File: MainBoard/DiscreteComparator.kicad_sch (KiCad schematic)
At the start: 27 parts, among them Q17 BC557, Q18 BC557, Q19 BC557, Q20 BC557, Q21 BC557, Q22 BC557, Q23 BC557, Q24 BC557, Q25 BC557, Q26 BC547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

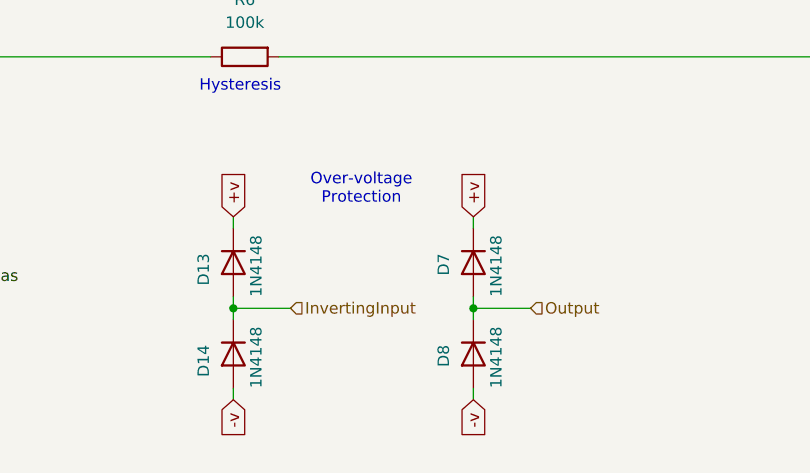
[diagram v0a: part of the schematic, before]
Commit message: added over-voltage protection on all inputs and outputs
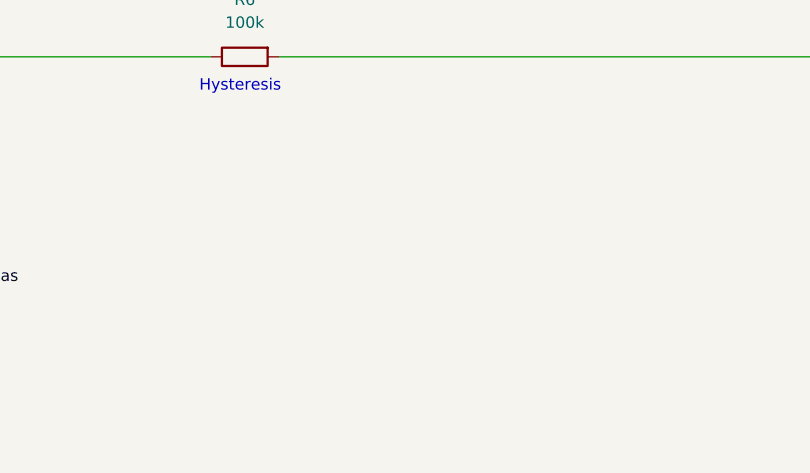
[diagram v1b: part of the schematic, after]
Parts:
- removed D13, D14, D7, D8: 1N4148, Diode_THT:D_DO-35_SOD27_P7.62mm_Horizontal, symbol Device:D
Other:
- note removed: "Over-voltage Protection"

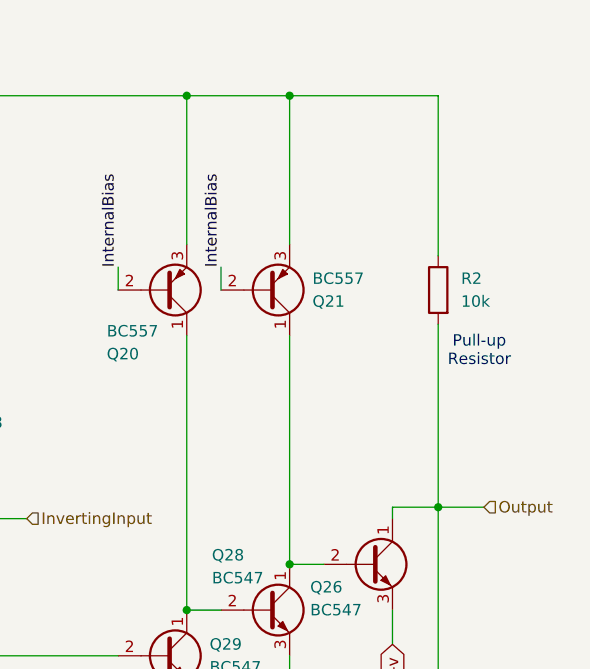
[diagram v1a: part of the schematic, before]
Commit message: moved pull up resistor out of the comparator and into the main scheamtic
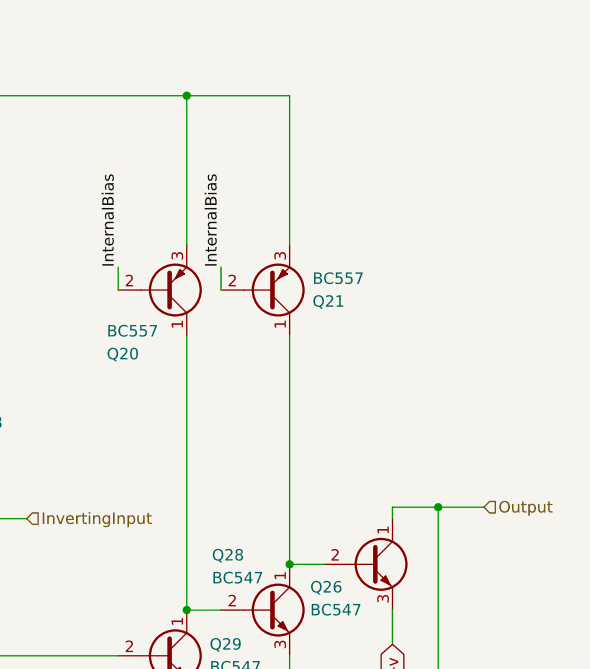
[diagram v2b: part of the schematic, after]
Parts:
- removed R2: 10k, Resistor_THT:R_Axial_DIN0207_L6.3mm_D2.5mm_P7.62mm_Horizontal, symbol Device:R
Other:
- note removed: "Pull-up Resistor"
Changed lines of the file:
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@@
-		)
-	)
-	(text "Pull-up\nResistor"
-		(exclude_from_sim no)
-		(at 207.772 52.578 0)
-		(effects
-			(font
-				(size 1.27 1.27)
-			)
 		)
 	)
@@
 		(color 0 0 0 0)
 	)
-	(junction
-		(at 186.69 24.13)
-		(diameter 0)
-		(color 0 0 0 0)
-	)
 	(wire
 		(pts
@@
 	(wire
 		(pts
-			(xy 203.2 24.13) (xy 203.2 41.91)
-		)
-		(stroke
-			(width 0)
-			(type default)
-		)
-	)
-	(wire
-		(pts
 			(xy 76.2 63.5) (xy 76.2 71.12)
 		)
@@
 	(wire
 		(pts
-			(xy 186.69 24.13) (xy 203.2 24.13)
-		)
-		(stroke
-			(width 0)
-			(type default)
-		)
-	)
-	(wire
-		(pts
 			(xy 87.63 63.5) (xy 87.63 66.04)
 		)
@@
 		(pts
 			(xy 119.38 21.59) (xy 119.38 24.13)
-		)
-		(stroke
-			(width 0)
-			(type default)
-		)
-	)
-	(wire
-		(pts
-			(xy 203.2 49.53) (xy 203.2 69.85)
 		)
 		(stroke
@@
 					(unit 1)
 				)
-			)
-		)
-	)
-	(symbol
-		(lib_id "Device:R")
-		(at 203.2 45.72 0)
-		(mirror y)
-		(unit 1)
-		(exclude_from_sim no)
-		(in_bom yes)
-		(on_board yes)
-		(dnp no)
-		(fields_autoplaced yes)
-		(property "Reference" "R2"
-			(at 205.74 44.4499 0)
-			(effects
-				(font
-					(size 1.27 1.27)
-				)
-				(justify right)
-			)
-		)
-		(property "Value" "10k"
-			(at 205.74 46.9899 0)
-			(effects
-				(font
-					(size 1.27 1.27)
-				)
-				(justify right)
-			)
-		)
-		(property "Footprint" "Resistor_THT:R_Axial_DIN0207_L6.3mm_D2.5mm_P7.62mm_Horizontal"
-			(at 204.978 45.72 90)
-			(effects
-				(font
-					(size 1.27 1.27)
-				)
-				(hide yes)
-			)
-		)
-		(property "Datasheet" "~"
-			(at 203.2 45.72 0)
-			(effects
-				(font
-					(size 1.27 1.27)
-				)
-				(hide yes)
-			)
-		)
-		(property "Description" "Resistor"
-			(at 203.2 45.72 0)
-			(effects
-				(font
-					(size 1.27 1.27)
-				)
-				(hide yes)
-			)
-		)
-		(pin "2"
-		)
-		(pin "1"
-		)
-		(instances
-			(project "MainBoard"
-				(path "/352c6875-c6d9-4d1a-ab6d-2f7b57ab28ef/53fe062f-4a00-461a-aeab-8f6e5d0d03e8"
-					(reference "R2")
-					(unit 1)
-				)
-				(path "/352c6875-c6d9-4d1a-ab6d-2f7b57ab28ef/db8f590d-63c1-489f-a9c8-ba7af9ba10fc"
-					(reference "R3")
-					(unit 1)
-				)

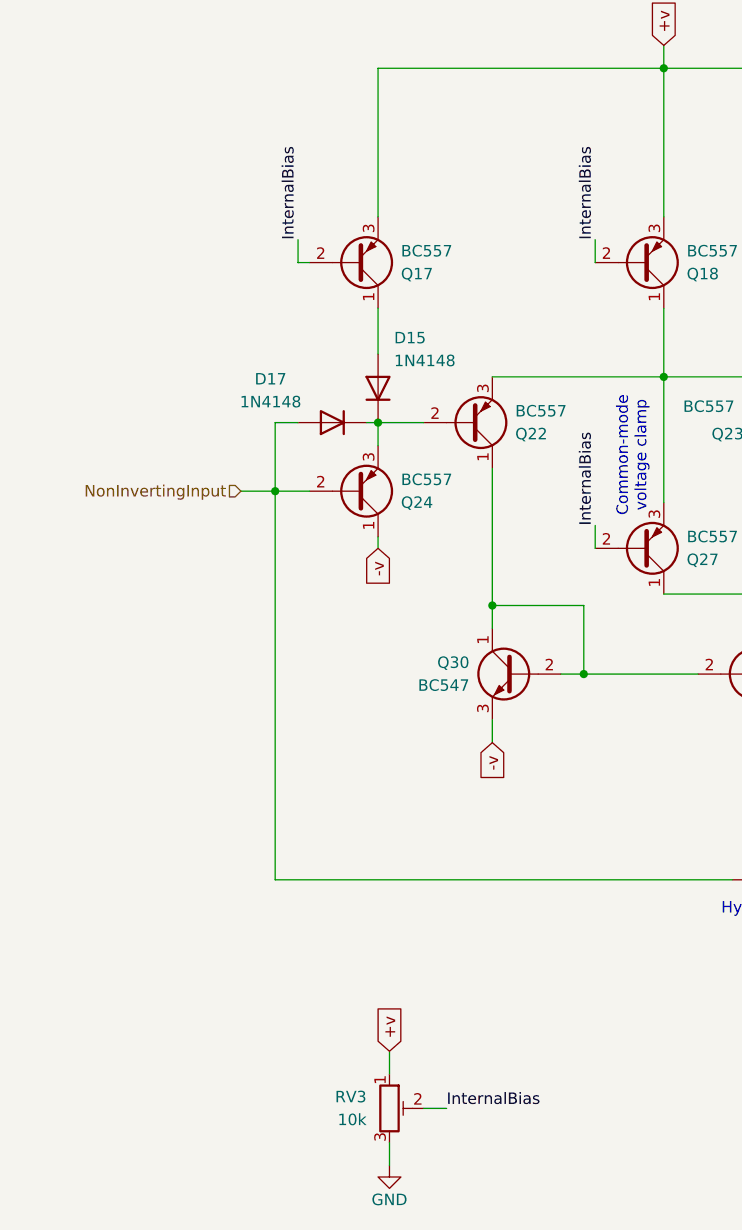
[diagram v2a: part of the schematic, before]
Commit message: added current limiting resistors to all inputs and outputs -- but currently having problem with the J8 normalled connection so leaving that out for now
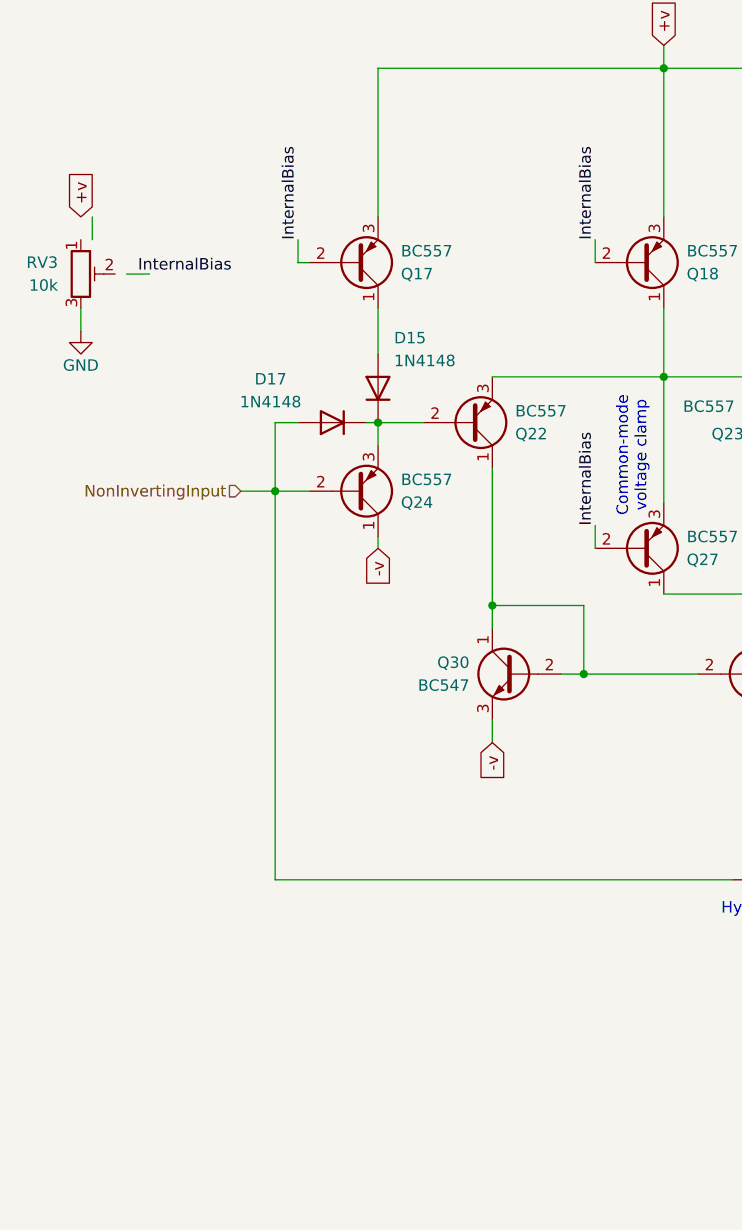
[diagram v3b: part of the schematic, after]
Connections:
- net +v: no longer RV3.1
- net InternalBias: no longer RV3.2
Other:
- moved on the sheet: RV3
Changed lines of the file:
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@@
 	(wire
 		(pts
-			(xy 92.71 139.7) (xy 95.25 139.7)
+			(xy 59.69 46.99) (xy 62.23 46.99)
 		)
 		(stroke
@@
 	(wire
 		(pts
-			(xy 88.9 133.35) (xy 88.9 135.89)
+			(xy 55.88 40.64) (xy 55.88 43.18)
 		)
 		(stroke
@@
 	(wire
 		(pts
-			(xy 88.9 143.51) (xy 88.9 146.05)
+			(xy 54.61 50.8) (xy 54.61 53.34)
 		)
 		(stroke
@@
 	)
 	(label "InternalBias"
-		(at 95.25 139.7 0)
+		(at 60.96 46.99 0)
 		(effects
 			(font
@@
 	(global_label "+v"
 		(shape input)
-		(at 88.9 133.35 90)
+		(at 54.61 40.64 90)
 		(fields_autoplaced yes)
 		(effects
@@
 		)
 		(property "Intersheetrefs" "${INTERSHEET_REFS}"
-			(at 88.9 127.8248 90)
+			(at 54.61 35.1148 90)
 			(effects
 				(font
@@
 	(symbol
 		(lib_id "power:GND")
-		(at 88.9 146.05 0)
+		(at 54.61 53.34 0)
 		(unit 1)
 		(exclude_from_sim no)
@@
 		(dnp no)
 		(property "Reference" "#PWR010"
-			(at 88.9 152.4 0)
+			(at 54.61 59.69 0)
 			(effects
 				(font
@@
 		)
 		(property "Value" "GND"
-			(at 88.9 149.86 0)
+			(at 54.61 57.15 0)
 			(effects
 				(font
@@
 		)
 		(property "Footprint" ""
-			(at 88.9 146.05 0)
+			(at 54.61 53.34 0)
 			(effects
 				(font
@@
 		)
 		(property "Datasheet" ""
-			(at 88.9 146.05 0)
+			(at 54.61 53.34 0)
 			(effects
 				(font
@@
 		)
 		(property "Description" "Power symbol creates a global label with name \"GND\" , ground"
-			(at 88.9 146.05 0)
+			(at 54.61 53.34 0)
 			(effects
 				(font
@@
 	(symbol
 		(lib_id "Device:R_Potentiometer_Trim")
-		(at 88.9 139.7 0)
+		(at 54.61 46.99 0)
 		(unit 1)
 		(exclude_from_sim no)
@@
 		(fields_autoplaced yes)
 		(property "Reference" "RV3"
-			(at 86.36 138.4299 0)
+			(at 52.07 45.7199 0)
 			(effects
 				(font
@@
 		)
 		(property "Value" "10k"
-			(at 86.36 140.9699 0)
+			(at 52.07 48.2599 0)
 			(effects
 				(font
@@
 		)
 		(property "Footprint" "Potentiometer_THT:Potentiometer_TT_P0915N"
-			(at 88.9 139.7 0)
+			(at 54.61 46.99 0)
 			(effects
 				(font
@@
 		)
 		(property "Datasheet" "~"
-			(at 88.9 139.7 0)
+			(at 54.61 46.99 0)
 			(effects
 				(font
@@
 		)
 		(property "Description" "Trim-potentiometer"
-			(at 88.9 139.7 0)
+			(at 54.61 46.99 0)
 			(effects
 				(font
@@
 		)
 		(property "Sim.Library" "models/potentiometer.lib"
-			(at 88.9 139.7 0)
+			(at 54.61 46.99 0)
 			(effects
 				(font
@@
 		)
 		(property "Sim.Name" "POT"
-			(at 88.9 139.7 0)
+			(at 54.61 46.99 0)
 			(effects
 				(font
@@
 		)
 		(property "Sim.Device" "SUBCKT"
-			(at 88.9 139.7 0)
+			(at 54.61 46.99 0)
 			(effects
 				(font
@@
 		)
 		(property "Sim.Pins" "1=1 2=2 3=3"
-			(at 88.9 139.7 0)
+			(at 54.61 46.99 0)
 			(effects
 				(font
@@
 		)
 		(property "Sim.Params" "Rtot=10k w=0.9"
-			(at 88.9 139.7 0)
-			(effects
-				(font
+			(at 54.61 46.99 0)
+			(effects
+				(font

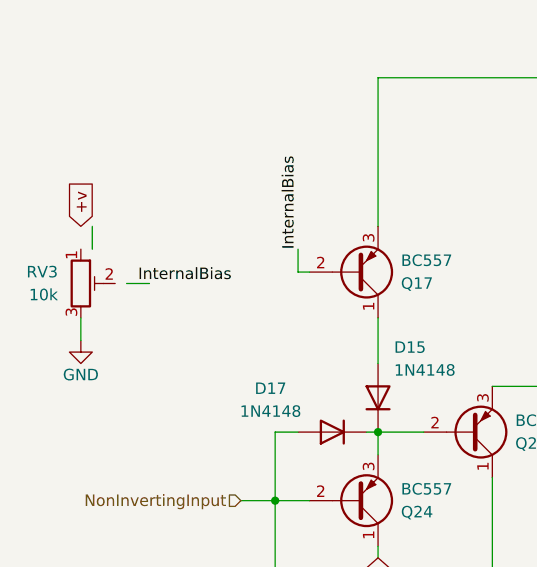
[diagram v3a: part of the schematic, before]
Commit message: added current limiting resistors to all inputs and outputs -- but currently having problem with the J8 normalled connection so leaving that out for now
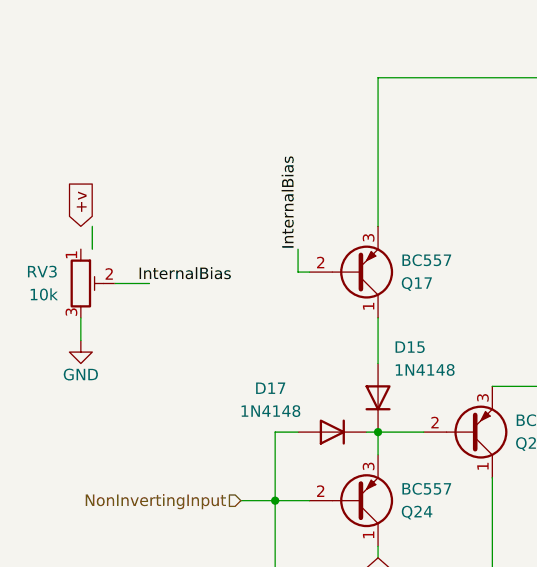
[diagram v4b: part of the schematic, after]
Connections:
- net InternalBias: now also RV3.2
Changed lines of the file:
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@@
-	(wire
-		(pts
-			(xy 59.69 46.99) (xy 62.23 46.99)
-		)
-		(stroke
-			(width 0)
-			(type default)
-		)
-	)
 	(wire
 		(pts
@@
 		)
 		(stroke
+			(width 0)
+			(type default)
+		)
+	)
+	(wire
+		(pts
+			(xy 58.42 46.99) (xy 62.23 46.99)
+		)
+		(stroke
